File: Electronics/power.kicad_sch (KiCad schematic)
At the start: 17 parts, among them J5 Conn_02x08_Odd_Even, U1 TL072

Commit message: deleting the plot
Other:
- company: (none) -> ©Dirty Dream - Nathanael Noir
- title: (none) -> CY3-FOLD VCO
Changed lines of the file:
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@@
 	(generator_version "10.0")
 	(paper "A4")
+	(title_block
+		(title "CY3-FOLD VCO")
+		(company "©Dirty Dream - Nathanael Noir")
+	)
 	(rectangle
 		(start 14.605 13.97)

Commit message: adding further testpoints
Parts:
- renumbered C17 to C11, C18 to C12, C11 to C13, C13 to C14, C12 to C16, C14 to C17, C16 to C18

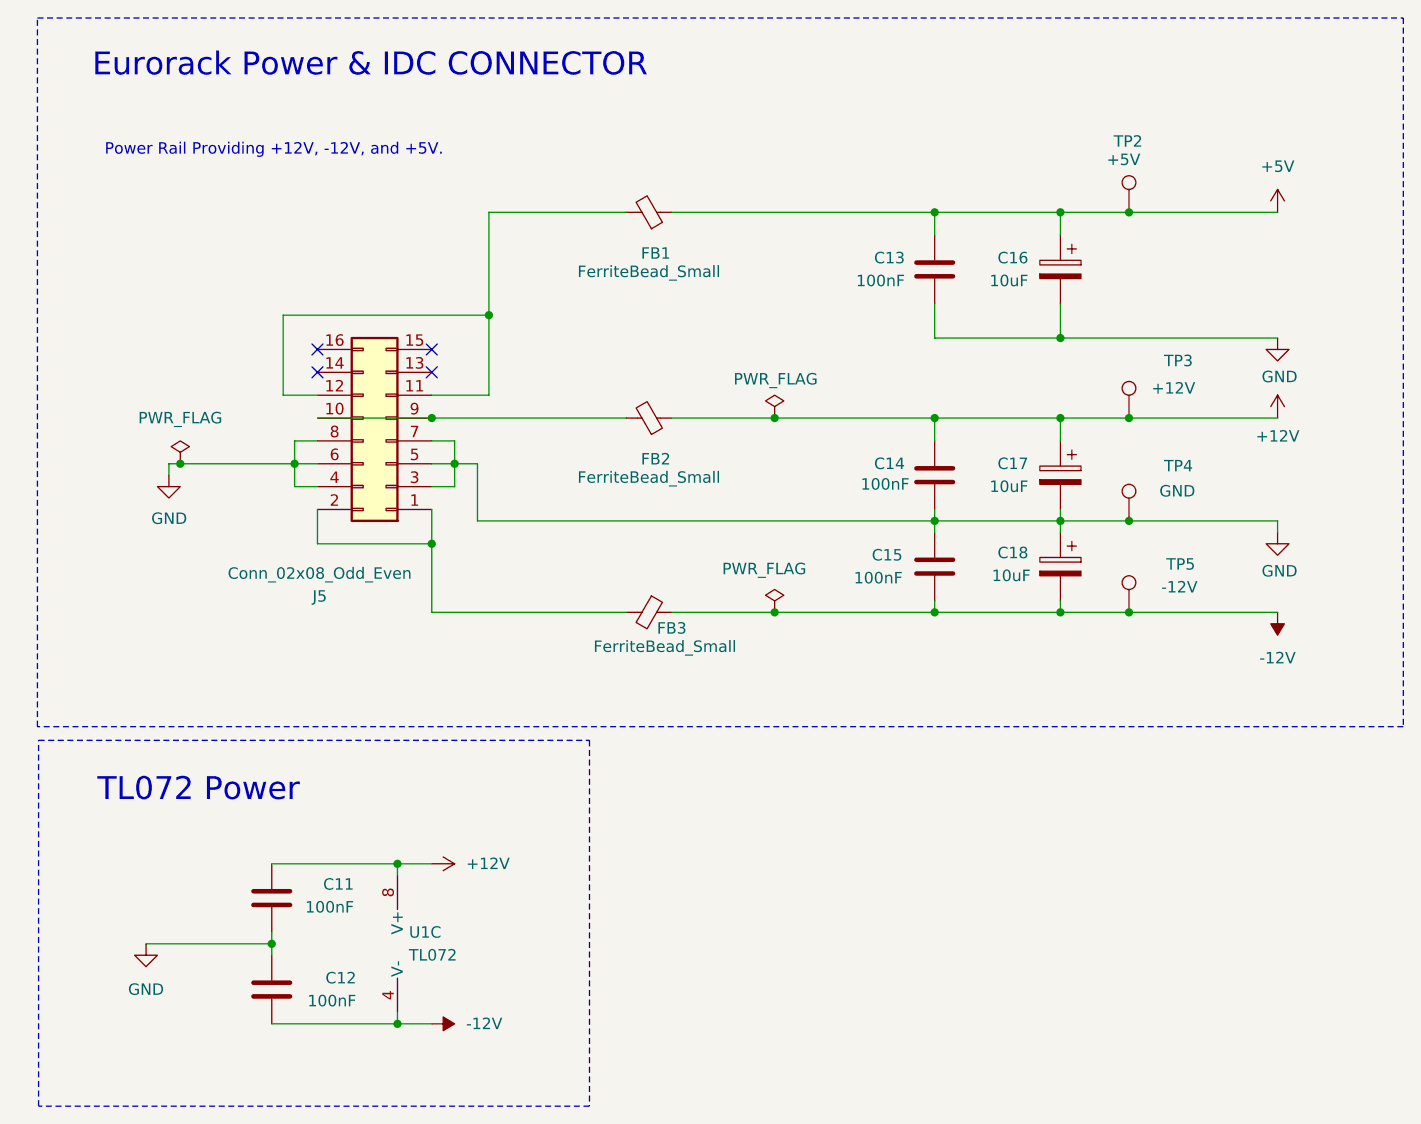
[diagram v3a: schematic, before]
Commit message: Add font configuration file for KiCad CLI reports
This commit introduces a new `fonts.conf` file to specify font directories and cache location for the KiCad CLI reports. The configuration includes standard system font directories as well as a user-specific font directory.
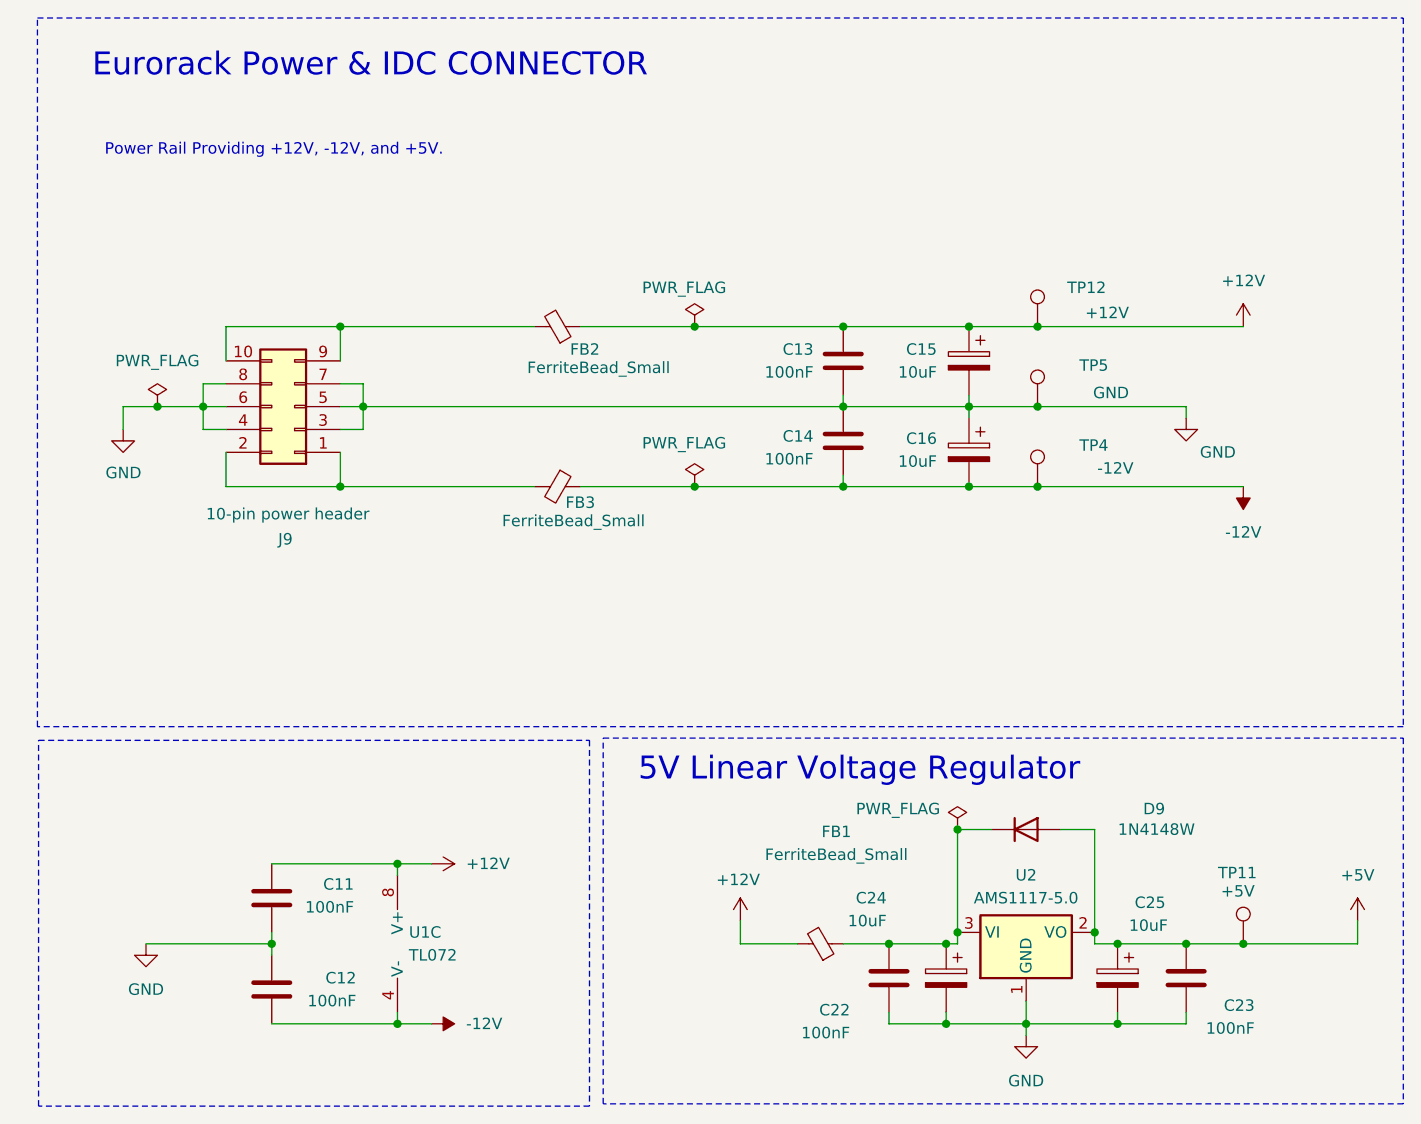
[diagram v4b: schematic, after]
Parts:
- removed C15: 100nF, Capacitor_SMD:C_0805_2012Metric_Pad1.18x1.45mm_HandSolder, symbol Device:C
- removed C17, C18: 10uF, Capacitor_SMD:CP_Elec_5x5.4, symbol Device:C_Polarized
- removed J5: Conn_02x08_Odd_Even, Connector_IDC:IDC-Header_2x08_P2.54mm_Vertical, symbol Connector_Generic:Conn_02x08_Odd_Even
- removed TP2: +5V, TestPoint:TestPoint_Pad_D1.5mm, symbol Connector:TestPoint
- removed TP3: +12V, TestPoint:TestPoint_Pad_D1.5mm, symbol Connector:TestPoint
- added C15, C24, C25: 10uF, Capacitor_SMD:CP_Elec_5x5.4, symbol Device:C_Polarized
- added C22, C23: 100nF, Capacitor_SMD:C_0805_2012Metric_Pad1.18x1.45mm_HandSolder, symbol Device:C
- added D9: 1N4148W, Diode_SMD:D_SOD-123, symbol Diode:1N4148W
- added J9: 10-pin power header, Connector_IDC:IDC-Header_2x05_P2.54mm_Vertical, symbol Connector_Generic:Conn_02x05_Odd_Even
- added TP11: +5V, TestPoint:TestPoint_Pad_D1.5mm, symbol Connector:TestPoint
- added TP12: +12V, TestPoint:TestPoint_Pad_D1.5mm, symbol Connector:TestPoint
- added U2: AMS1117-5.0, Package_TO_SOT_SMD:SOT-223-3_TabPin2, symbol Regulator_Linear:AMS1117-5.0
- TP4: value GND -> -12V
- TP5: value -12V -> GND
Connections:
- net +12V: now also C13.1, FB1.2, C15.1, TP12.1; no longer C14.1
- net +5V: now also C23.1, C25.1, D9.2 (A), TP11.1, U2.2 (VO); no longer C13.1, C16.1, FB1.1
- net -12V: now also C14.2, C16.2, TP4.1; no longer TP5.1
- net GND: now also C14.1, C16.1, TP5.1, C15.2, C22.2, C23.2, C24.2, C25.2, J9.3 (Pin_3), J9.4 (Pin_4), J9.5 (Pin_5), J9.6 (Pin_6), J9.7 (Pin_7), J9.8 (Pin_8), U2.1 (GND); no longer C14.2, C16.2, TP4.1
- net at FB2.2: now also J9.10 (Pin_10), J9.9 (Pin_9)
- net at FB3.2: now also J9.1 (Pin_1), J9.2 (Pin_2)
- new net: C22.1, C24.1, D9.1 (K), FB1.1, U2.3 (VI)
- no-connect marks 4 -> 0
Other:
- note added: "5V Linear Voltage Regulator"
- note removed: "TL072 Power"

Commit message: starting pcb
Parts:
- removed C22: 100nF, Capacitor_SMD:C_0805_2012Metric_Pad1.18x1.45mm_HandSolder, symbol Device:C
- removed C24: 10uF, Capacitor_SMD:CP_Elec_5x5.4, symbol Device:C_Polarized
- removed FB1: FerriteBead_Small, Inductor_SMD:L_0805_2012Metric_Pad1.05x1.20mm_HandSolder, symbol Device:FerriteBead_Small
- added C24: 100nF, Capacitor_SMD:C_0805_2012Metric_Pad1.18x1.45mm_HandSolder, symbol Device:C
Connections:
- net +12V: now also D9.1 (K), U2.3 (VI), C24.1
- net GND: now also C24.2
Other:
- moved on the sheet: C23, C25, TP11

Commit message: Adding Silkscreen symbols
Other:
- company: ©Dirty Dream - Nathanael Noir -> © Dirty Dream – Nathanael Noir
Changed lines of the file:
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@@
 	(title_block
 		(title "CY3-FOLD VCO")
-		(company "©Dirty Dream - Nathanael Noir")
+		(date "2026-06-21")
+		(rev "v1.0")
+		(company "© Dirty Dream – Nathanael Noir")
 	)
 	(rectangle
